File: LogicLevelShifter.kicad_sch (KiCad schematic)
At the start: 3 parts, among them Q1 Transistor-FET-.2A-2.6V-TH

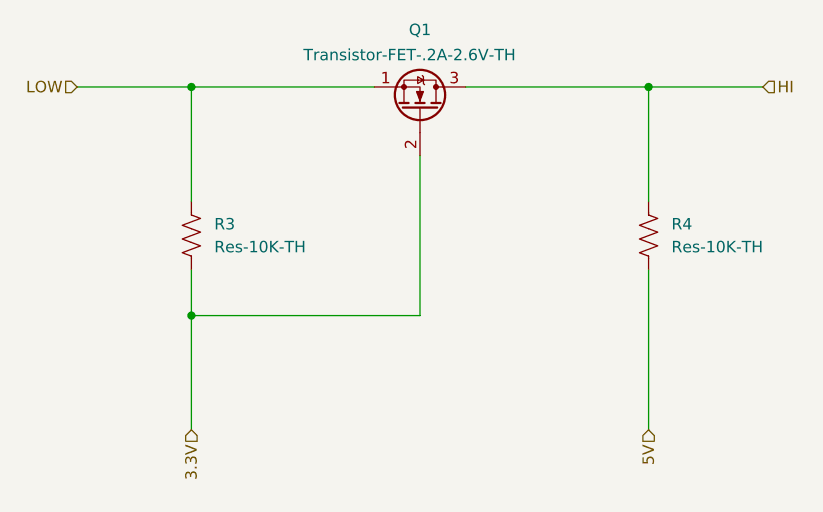
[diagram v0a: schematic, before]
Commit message: Added appropriate logic level shifter based on 2N7000 design.
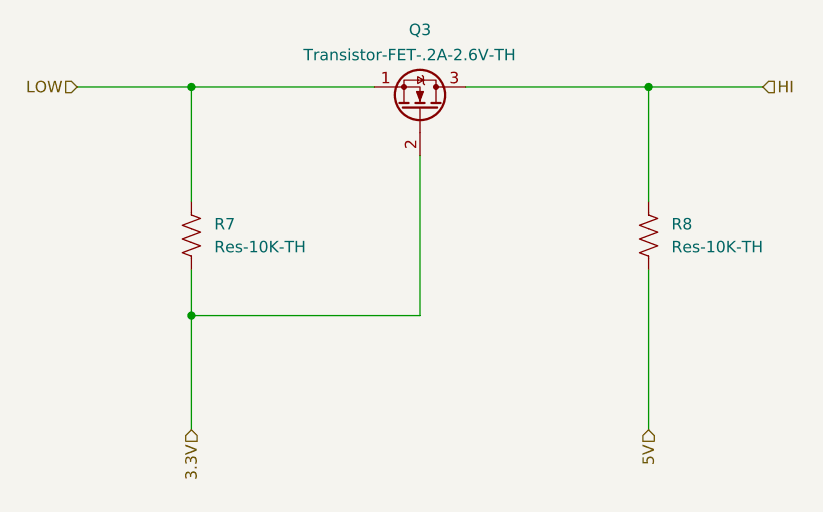
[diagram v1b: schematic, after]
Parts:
- renumbered Q1 to Q3, R3 to R7, R4 to R8
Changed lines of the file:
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@@
 		(on_board yes)
 		(dnp no)
-		(property "Reference" "Q1"
+		(property "Reference" "Q3"
 			(at 114.3 82.55 90)
 			(effects
@@
 		(instances
 			(project "Arduino Mega CMRI WiFi Shield"
-				(path "/b5f17be1-57ef-4578-85e6-f9a5d0b9e453/24ca8a12-b010-4647-93e9-91c3de63f992/6676a218-c0f2-4979-b10d-0479ba020484"
+				(path "/b5f17be1-57ef-4578-85e6-f9a5d0b9e453/24ca8a12-b010-4647-93e9-91c3de63f992/c903c757-f01e-4459-b19e-90070c05d630"
+					(reference "Q1")
+					(unit 1)
+				)
+				(path "/b5f17be1-57ef-4578-85e6-f9a5d0b9e453/24ca8a12-b010-4647-93e9-91c3de63f992/f05ee424-7b6e-4191-b4ed-34bc530e2052"
 					(reference "Q3")
 					(unit 1)
 				)
-				(path "/b5f17be1-57ef-4578-85e6-f9a5d0b9e453/24ca8a12-b010-4647-93e9-91c3de63f992/74f7e823-7471-4755-83fe-f0f1f6e06ad4"
-					(reference "Q1")
-					(unit 1)
-				)
-				(path "/b5f17be1-57ef-4578-85e6-f9a5d0b9e453/24ca8a12-b010-4647-93e9-91c3de63f992/a8c88e65-1ee7-4962-bcaa-9ac4e8b0feb7"
+				(path "/b5f17be1-57ef-4578-85e6-f9a5d0b9e453/24ca8a12-b010-4647-93e9-91c3de63f992/f8156dbb-b993-44ba-a822-820636299b35"
 					(reference "Q2")
 					(unit 1)
@@
 		(dnp no)
 		(fields_autoplaced yes)
-		(property "Reference" "R4"
+		(property "Reference" "R8"
 			(at 142.24 104.1399 0)
 			(effects
@@
 		(instances
 			(project "Arduino Mega CMRI WiFi Shield"
-				(path "/b5f17be1-57ef-4578-85e6-f9a5d0b9e453/24ca8a12-b010-4647-93e9-91c3de63f992/6676a218-c0f2-4979-b10d-0479ba020484"
+				(path "/b5f17be1-57ef-4578-85e6-f9a5d0b9e453/24ca8a12-b010-4647-93e9-91c3de63f992/c903c757-f01e-4459-b19e-90070c05d630"
+					(reference "R4")
+					(unit 1)
+				)
+				(path "/b5f17be1-57ef-4578-85e6-f9a5d0b9e453/24ca8a12-b010-4647-93e9-91c3de63f992/f05ee424-7b6e-4191-b4ed-34bc530e2052"
 					(reference "R8")
 					(unit 1)
 				)
-				(path "/b5f17be1-57ef-4578-85e6-f9a5d0b9e453/24ca8a12-b010-4647-93e9-91c3de63f992/74f7e823-7471-4755-83fe-f0f1f6e06ad4"
-					(reference "R4")
-					(unit 1)
-				)
-				(path "/b5f17be1-57ef-4578-85e6-f9a5d0b9e453/24ca8a12-b010-4647-93e9-91c3de63f992/a8c88e65-1ee7-4962-bcaa-9ac4e8b0feb7"
+				(path "/b5f17be1-57ef-4578-85e6-f9a5d0b9e453/24ca8a12-b010-4647-93e9-91c3de63f992/f8156dbb-b993-44ba-a822-820636299b35"
 					(reference "R6")
 					(unit 1)
@@
 		(dnp no)
 		(fields_autoplaced yes)
-		(property "Reference" "R3"
+		(property "Reference" "R7"
 			(at 91.44 104.1399 0)
 			(effects
@@
 		(instances
 			(project "Arduino Mega CMRI WiFi Shield"
-				(path "/b5f17be1-57ef-4578-85e6-f9a5d0b9e453/24ca8a12-b010-4647-93e9-91c3de63f992/6676a218-c0f2-4979-b10d-0479ba020484"
+				(path "/b5f17be1-57ef-4578-85e6-f9a5d0b9e453/24ca8a12-b010-4647-93e9-91c3de63f992/c903c757-f01e-4459-b19e-90070c05d630"
+					(reference "R2")
+					(unit 1)
+				)
+				(path "/b5f17be1-57ef-4578-85e6-f9a5d0b9e453/24ca8a12-b010-4647-93e9-91c3de63f992/f05ee424-7b6e-4191-b4ed-34bc530e2052"
 					(reference "R7")
 					(unit 1)
 				)
-				(path "/b5f17be1-57ef-4578-85e6-f9a5d0b9e453/24ca8a12-b010-4647-93e9-91c3de63f992/74f7e823-7471-4755-83fe-f0f1f6e06ad4"
-					(reference "R3")
-					(unit 1)
-				)
-				(path "/b5f17be1-57ef-4578-85e6-f9a5d0b9e453/24ca8a12-b010-4647-93e9-91c3de63f992/a8c88e65-1ee7-4962-bcaa-9ac4e8b0feb7"
+				(path "/b5f17be1-57ef-4578-85e6-f9a5d0b9e453/24ca8a12-b010-4647-93e9-91c3de63f992/f8156dbb-b993-44ba-a822-820636299b35"
 					(reference "R5")
 					(unit 1)

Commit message: Updates look good, promoted to v1.2.
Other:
- title: ESP8266 ESP-01 WiFi Module -> Arduino Mega CMRI WiFi Shield
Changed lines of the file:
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@@
 	(paper "A4")
 	(title_block
-		(title "ESP8266 ESP-01 WiFi Module")
-		(date "2026-01-30")
-		(rev "1.1")
+		(title "Arduino Mega CMRI WiFi Shield")
+		(date "2026-02-10")
+		(rev "1.2")
 	)
 	(junction
